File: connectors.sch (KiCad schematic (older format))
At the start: 15 parts, among them J1 2001-1-2-21-00-BK, P2 USB_A, P3 CAM1, Q3 2N7002P.215

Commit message: Assigned footprints to most components
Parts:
- removed D2, D3: BAT54, symbol D_Schottky
- added D2, D3: BAT54, TO_SOT_Packages_SMD:SOT-23, symbol D_Schottky_AAK
- C16: footprint (none) -> Capacitors_Tantalum_SMD:CP_Tantalum_Case-C_EIA-6032-28_Reflow
- C17: footprint (none) -> Capacitors_SMD:C_0603_HandSoldering
- D4, D5, D6, D7, Q3: footprint (none) -> TO_SOT_Packages_SMD:SOT-23
- P2: value USB_A -> HOST; footprint (none) -> Connectors:USB_A
- R4, R5, R6: footprint (none) -> Resistors_SMD:R_0603_HandSoldering
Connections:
- no-connect marks 1 -> 3
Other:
- moved on the sheet: C16, P2
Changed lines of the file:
@@
 L GND #PWR050
 U 1 1 5C1263C9
-P 1350 1650
-F 0 "#PWR050" H 1350 1400 50  0001 C CNN
-F 1 "GND" H 1350 1500 50  0000 C CNN
-F 2 "" H 1350 1650 50  0000 C CNN
-F 3 "" H 1350 1650 50  0000 C CNN
-	1    1350 1650
+P 1350 1700
+F 0 "#PWR050" H 1350 1450 50  0001 C CNN
+F 1 "GND" H 1350 1550 50  0000 C CNN
+F 2 "" H 1350 1700 50  0000 C CNN
+F 3 "" H 1350 1700 50  0000 C CNN
+	1    1350 1700
 	1    0    0    -1
 $EndComp
@@
 L GND #PWR051
 U 1 1 5C1263E1
-P 1600 1650
-F 0 "#PWR051" H 1600 1400 50  0001 C CNN
-F 1 "GND" H 1600 1500 50  0000 C CNN
-F 2 "" H 1600 1650 50  0000 C CNN
-F 3 "" H 1600 1650 50  0000 C CNN
-	1    1600 1650
-	1    0    0    -1
-$EndComp
-Text GLabel 1150 1150 3    60   Input ~ 0
+P 1600 1700
+F 0 "#PWR051" H 1600 1450 50  0001 C CNN
+F 1 "GND" H 1600 1550 50  0000 C CNN
+F 2 "" H 1600 1700 50  0000 C CNN
+F 3 "" H 1600 1700 50  0000 C CNN
+	1    1600 1700
+	1    0    0    -1
+$EndComp
+Text GLabel 1150 1200 3    60   Input ~ 0
 USB_DM
-Text GLabel 1250 1150 3    60   Input ~ 0
+Text GLabel 1250 1200 3    60   Input ~ 0
 USB_DP
 $Comp
 L +5V #PWR052
 U 1 1 5C126DDC
-P 650 700
-F 0 "#PWR052" H 650 550 50  0001 C CNN
-F 1 "+5V" H 650 840 50  0000 C CNN
-F 2 "" H 650 700 50  0000 C CNN
-F 3 "" H 650 700 50  0000 C CNN
-	1    650  700
+P 550 700
+F 0 "#PWR052" H 550 550 50  0001 C CNN
+F 1 "+5V" H 550 840 50  0000 C CNN
+F 2 "" H 550 700 50  0000 C CNN
+F 3 "" H 550 700 50  0000 C CNN
+	1    550  700
 	1    0    0    -1
 $EndComp
@@
 L CP1 C16
 U 1 1 5C1275E4
-P 650 1400
-F 0 "C16" H 675 1500 50  0000 L CNN
-F 1 "10uF" H 675 1300 50  0000 L CNN
-F 2 "" H 650 1400 50  0000 C CNN
-F 3 "" H 650 1400 50  0000 C CNN
-	1    650  1400
+P 650 1450
+F 0 "C16" H 675 1550 50  0000 L CNN
+F 1 "10uF" H 675 1350 50  0000 L CNN
+F 2 "Capacitors_Tantalum_SMD:CP_Tantalum_Case-C_EIA-6032-28_Reflow" H 650 1450 50  0001 C CNN
+F 3 "" H 650 1450 50  0000 C CNN
+	1    650  1450
 	1    0    0    -1
 $EndComp
@@
 L GND #PWR053
 U 1 1 5C127628
-P 650 1650
-F 0 "#PWR053" H 650 1400 50  0001 C CNN
-F 1 "GND" H 650 1500 50  0000 C CNN
-F 2 "" H 650 1650 50  0000 C CNN
-F 3 "" H 650 1650 50  0000 C CNN
-	1    650  1650
+P 650 1700
+F 0 "#PWR053" H 650 1450 50  0001 C CNN
+F 1 "GND" H 650 1550 50  0000 C CNN
+F 2 "" H 650 1700 50  0000 C CNN
+F 3 "" H 650 1700 50  0000 C CNN
+	1    650  1700
 	1    0    0    -1
 $EndComp
@@
 F 0 "P3" H 2100 2850 50  0000 C CNN
 F 1 "CAM1" V 2200 1700 50  0000 C CNN
-F 2 "" H 2100 1700 50  0000 C CNN
+F 2 "" H 2100 1700 50  0001 C CNN
 F 3 "" H 2100 1700 50  0000 C CNN
 	1    2100 1700
@@
 L USB_A P2
 U 1 1 5C12CE0A
-P 1250 750
-F 0 "P2" H 1450 550 50  0000 C CNN
-F 1 "USB_A" H 1200 950 50  0000 C CNN
-F 2 "" V 1200 650 50  0000 C CNN
-F 3 "" V 1200 650 50  0000 C CNN
-	1    1250 750
+P 1250 800
+F 0 "P2" H 1450 600 50  0000 C CNN
+F 1 "HOST" H 1200 1000 50  0000 C CNN
+F 2 "Connectors:USB_A" V 1200 700 50  0001 C CNN
+F 3 "" V 1200 700 50  0000 C CNN
+	1    1250 800
 	1    0    0    -1
 $EndComp
@@
 F 0 "D4" H 6100 3350 50  0000 C CNN
 F 1 "BAV99" H 6050 3550 50  0000 C CNN
-F 2 "" H 6050 3450 50  0000 C CNN
+F 2 "TO_SOT_Packages_SMD:SOT-23" H 6050 3450 50  0001 C CNN
 F 3 "" H 6050 3450 50  0000 C CNN
 	1    6050 3450
@@
 $EndComp
 $Comp
-L D_Schottky D3
-U 1 1 5C12B9C1
-P 5450 1550
-F 0 "D3" H 5450 1650 50  0000 C CNN
-F 1 "BAT54" H 5450 1450 50  0000 C CNN
-F 2 "" H 5450 1550 50  0000 C CNN
-F 3 "" H 5450 1550 50  0000 C CNN
-	1    5450 1550
-	0    -1   -1   0
-$EndComp
-$Comp
 L +5V #PWR056
 U 1 1 5C12BC08
-P 5450 700
-F 0 "#PWR056" H 5450 550 50  0001 C CNN
-F 1 "+5V" H 5450 840 50  0000 C CNN
-F 2 "" H 5450 700 50  0000 C CNN
-F 3 "" H 5450 700 50  0000 C CNN
-	1    5450 700
+P 5350 700
+F 0 "#PWR056" H 5350 550 50  0001 C CNN
+F 1 "+5V" H 5350 840 50  0000 C CNN
+F 2 "" H 5350 700 50  0000 C CNN
+F 3 "" H 5350 700 50  0000 C CNN
+	1    5350 700
 	1    0    0    -1
 $EndComp
@@
 F 0 "C17" H 5025 3550 50  0000 L CNN
 F 1 "100nF" H 5025 3350 50  0000 L CNN
-F 2 "" H 5038 3300 50  0000 C CNN
+F 2 "Capacitors_SMD:C_0603_HandSoldering" H 5038 3300 50  0001 C CNN
 F 3 "" H 5000 3450 50  0000 C CNN
 	1    5000 3450
@@
 F 0 "D5" H 6600 3350 50  0000 C CNN
 F 1 "BAV99" H 6550 3550 50  0000 C CNN
-F 2 "" H 6550 3450 50  0000 C CNN
+F 2 "TO_SOT_Packages_SMD:SOT-23" H 6550 3450 50  0001 C CNN
 F 3 "" H 6550 3450 50  0000 C CNN
 	1    6550 3450
@@
 F 0 "D6" H 7100 3350 50  0000 C CNN
 F 1 "BAV99" H 7050 3550 50  0000 C CNN
-F 2 "" H 7050 3450 50  0000 C CNN
+F 2 "TO_SOT_Packages_SMD:SOT-23" H 7050 3450 50  0001 C CNN
 F 3 "" H 7050 3450 50  0000 C CNN
 	1    7050 3450
@@
 F 0 "R4" V 6330 1550 50  0000 C CNN
 F 1 "1.8K" V 6250 1550 50  0000 C CNN
-F 2 "" V 6180 1550 50  0000 C CNN
+F 2 "Resistors_SMD:R_0603_HandSoldering" V 6180 1550 50  0001 C CNN
 F 3 "" H 6250 1550 50  0000 C CNN
 	1    6250 1550
@@
 F 0 "R5" V 6830 1550 50  0000 C CNN
 F 1 "1.8K" V 6750 1550 50  0000 C CNN
-F 2 "" V 6680 1550 50  0000 C CNN
+F 2 "Resistors_SMD:R_0603_HandSoldering" V 6680 1550 50  0001 C CNN
 F 3 "" H 6750 1550 50  0000 C CNN
 	1    6750 1550
@@
 HDMI_CLK_N
 $Comp
-L D_Schottky D2
-U 1 1 5C132132
-P 650 900
-F 0 "D2" H 650 1000 50  0000 C CNN
-F 1 "BAT54" H 650 800 50  0000 C CNN
-F 2 "" H 650 900 50  0000 C CNN
-F 3 "" H 650 900 50  0000 C CNN
-	1    650  900
-	0    -1   -1   0
-$EndComp
-$Comp
 L Q_NMOS_GSD Q3
 U 1 1 5C13782A
@@
 F 0 "Q3" H 8250 3500 50  0000 L CNN
 F 1 "2N7002P.215" H 8250 3400 50  0000 L CNN
-F 2 "" H 8250 3550 50  0000 C CNN
+F 2 "TO_SOT_Packages_SMD:SOT-23" H 8250 3550 50  0001 C CNN
 F 3 "" H 8050 3450 50  0000 C CNN
 	1    8050 3450
@@
 F 0 "R6" V 8230 2950 50  0000 C CNN
 F 1 "100K" V 8150 2950 50  0000 C CNN
-F 2 "" V 8080 2950 50  0000 C CNN
+F 2 "Resistors_SMD:R_0603_HandSoldering" V 8080 2950 50  0001 C CNN
 F 3 "" H 8150 2950 50  0000 C CNN
 	1    8150 2950
@@
 Connection ~ 5450 2850
 Wire Wire Line
-	5450 2850 5450 1700
-Wire Wire Line
-	5450 1400 5450 700
+	5350 1400 5350 700
 Wire Wire Line
 	4500 2250 4700 2250
@@
 	2300 650  2400 650
 Wire Wire Line
-	650  1550 650  1650
-Connection ~ 650  1150
-Wire Wire Line
-	650  750  650  700
-Wire Wire Line
-	650  1050 650  1250
-Wire Wire Line
-	650  1150 1050 1150
-Wire Wire Line
-	1050 1150 1050 1050
-Wire Wire Line
-	1250 1050 1250 1150
-Wire Wire Line
-	1150 1050 1150 1150
-Wire Wire Line
-	1600 650  1600 1650
-Wire Wire Line
-	1550 650  1600 650
-Wire Wire Line
-	1350 1650 1350 1050
+	650  1600 650  1700
+Connection ~ 650  1200
+Wire Wire Line
+	550  750  550  700
+Wire Wire Line
+	650  1100 650  1300
+Wire Wire Line
+	650  1200 1050 1200
+Wire Wire Line
+	1050 1200 1050 1100
+Wire Wire Line
+	1250 1100 1250 1200
+Wire Wire Line
+	1150 1100 1150 1200
+Wire Wire Line
+	1600 700  1600 1700
+Wire Wire Line
+	1550 700  1600 700
+Wire Wire Line
+	1350 1700 1350 1100
 $Comp
 L D_x2_Serial_AKC D7
@@
 F 0 "D7" H 7600 3350 50  0000 C CNN
 F 1 "BAV99" H 7550 3550 50  0000 C CNN
-F 2 "" H 7550 3450 50  0000 C CNN
+F 2 "TO_SOT_Packages_SMD:SOT-23" H 7550 3450 50  0001 C CNN
 F 3 "" H 7550 3450 50  0000 C CNN
 	1    7550 3450
@@
 L PWR_FLAG #FLG067
 U 1 1 5C13FE61
-P 850 750
-F 0 "#FLG067" H 850 845 50  0001 C CNN
-F 1 "PWR_FLAG" V 900 600 50  0000 C CNN
-F 2 "" H 850 750 50  0000 C CNN
-F 3 "" H 850 750 50  0000 C CNN
-	1    850  750
-	1    0    0    -1
-$EndComp
-Wire Wire Line
-	850  750  850  1150
-Connection ~ 850  1150
+P 850 800
+F 0 "#FLG067" H 850 895 50  0001 C CNN
+F 1 "PWR_FLAG" V 900 650 50  0000 C CNN
+F 2 "" H 850 800 50  0000 C CNN
+F 3 "" H 850 800 50  0000 C CNN
+	1    850  800
+	1    0    0    -1
+$EndComp
+Wire Wire Line
+	850  800  850  1200
+Connection ~ 850  1200
+$Comp
+L D_Schottky_AAK D3
+U 1 1 5C147BC1
+P 5450 1600
+F 0 "D3" H 5450 1700 50  0000 C CNN
+F 1 "BAT54" H 5450 1500 50  0000 C CNN
+F 2 "TO_SOT_Packages_SMD:SOT-23" H 5450 1600 50  0001 C CNN
+F 3 "" H 5450 1600 50  0000 C CNN
+	1    5450 1600
+	0    -1   -1   0
+$EndComp
+Wire Wire Line
+	5450 1750 5450 2850
+NoConn ~ 5450 1400
+$Comp
+L D_Schottky_AAK D2
+U 1 1 5C1483E3
+P 650 950
+F 0 "D2" H 650 1050 50  0000 C CNN
+F 1 "BAT54" H 650 850 50  0000 C CNN
+F 2 "TO_SOT_Packages_SMD:SOT-23" H 650 950 50  0001 C CNN
+F 3 "" H 650 950 50  0000 C CNN
+	1    650  950
+	0    -1   -1   0
+$EndComp
+NoConn ~ 650  750
 $EndSCHEMATC

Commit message: Added camera connector footprint
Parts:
- J1: footprint digikey-footprints:HDMI_Mini_Female_2001-1-2-21-00-BK -> digikey-footprints:HDMI_Female_DC3RX19JA3R1700
- P3: footprint (none) -> ffc_conn:FPC_22
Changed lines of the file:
@@
 F 0 "P3" H 2100 2850 50  0000 C CNN
 F 1 "CAM1" V 2200 1700 50  0000 C CNN
-F 2 "" H 2100 1700 50  0001 C CNN
+F 2 "ffc_conn:FPC_22" H 2100 1700 50  0001 C CNN
 F 3 "" H 2100 1700 50  0000 C CNN
 	1    2100 1700
@@
 F 0 "J1" H 3585 3545 60  0000 C CNN
 F 1 "2001-1-2-21-00-BK" V 3510 1095 60  0000 C CNN
-F 2 "digikey-footprints:HDMI_Mini_Female_2001-1-2-21-00-BK" H 4100 2250 60  0001 L CNN
+F 2 "digikey-footprints:HDMI_Female_DC3RX19JA3R1700" H 4100 2250 60  0001 L CNN
 F 3 "http://cnctech.us/pdfs/2001-1-2-21-00-BK.pdf" H 4100 2350 60  0001 L CNN
 F 4 "1175-1704-1-ND" H 4100 2450 60  0001 L CNN "Digi-Key_PN"

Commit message: Replaced HDMI connector
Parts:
- J1: footprint digikey-footprints:HDMI_Female_DC3RX19JA3R1700 -> HDMI_MOLEX:HDMI_MOLEX_471510001
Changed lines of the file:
@@
 F 0 "J1" H 3585 3545 60  0000 C CNN
 F 1 "2001-1-2-21-00-BK" V 3510 1095 60  0000 C CNN
-F 2 "digikey-footprints:HDMI_Female_DC3RX19JA3R1700" H 4100 2250 60  0001 L CNN
+F 2 "HDMI_MOLEX:HDMI_MOLEX_471510001" H 4100 2250 60  0001 L CNN
 F 3 "http://cnctech.us/pdfs/2001-1-2-21-00-BK.pdf" H 4100 2350 60  0001 L CNN
 F 4 "1175-1704-1-ND" H 4100 2450 60  0001 L CNN "Digi-Key_PN"

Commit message: Fixed fused
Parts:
- C17: footprint Capacitors_SMD:C_0603_HandSoldering -> Capacitors_SMD:C_0402
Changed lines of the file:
@@
 F 0 "C17" H 5025 3550 50  0000 L CNN
 F 1 "100nF" H 5025 3350 50  0000 L CNN
-F 2 "Capacitors_SMD:C_0603_HandSoldering" H 5038 3300 50  0001 C CNN
+F 2 "Capacitors_SMD:C_0402" H 5038 3300 50  0001 C CNN
 F 3 "" H 5000 3450 50  0000 C CNN
 	1    5000 3450

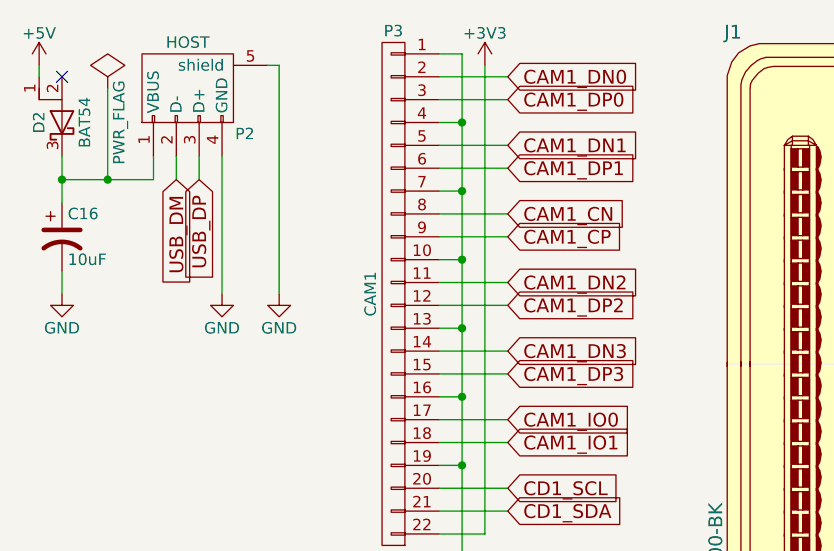
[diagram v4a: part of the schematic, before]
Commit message: Routed differential pairs for camera and HDMI
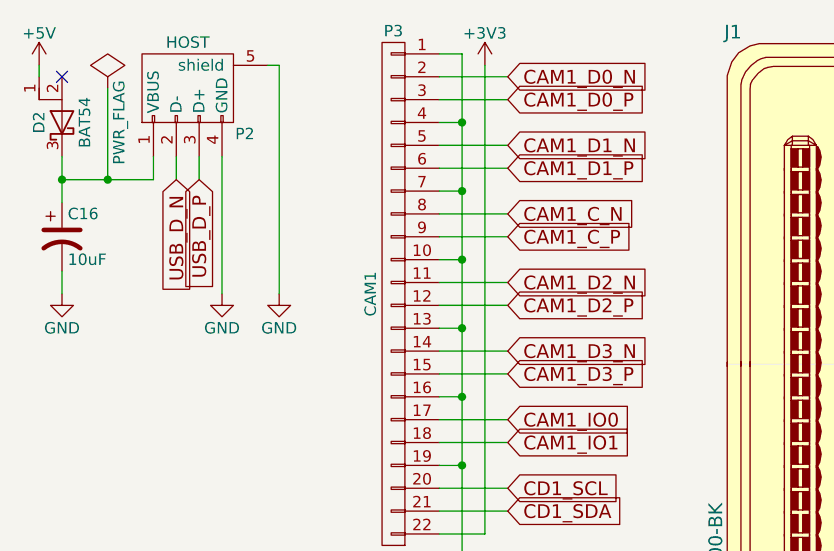
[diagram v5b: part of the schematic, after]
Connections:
- net CAM1_CN renamed CAM1_C_N
- net CAM1_CP renamed CAM1_C_P
- net CAM1_DN0 renamed CAM1_D0_N
- net CAM1_DN1 renamed CAM1_D1_N
- net CAM1_DN2 renamed CAM1_D2_N
- net CAM1_DN3 renamed CAM1_D3_N
- net CAM1_DP0 renamed CAM1_D0_P
- net CAM1_DP1 renamed CAM1_D1_P
- net CAM1_DP2 renamed CAM1_D2_P
- net CAM1_DP3 renamed CAM1_D3_P
- net USB_DM renamed USB_D_N
- net USB_DP renamed USB_D_P
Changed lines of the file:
@@
 $EndComp
 Text GLabel 1150 1200 3    60   Input ~ 0
-USB_DM
+USB_D_N
 Text GLabel 1250 1200 3    60   Input ~ 0
-USB_DP
+USB_D_P
 $Comp
 L +5V #PWR052
@@
 $EndComp
 Text GLabel 2600 750  2    60   Input ~ 0
-CAM1_DN0
+CAM1_D0_N
 Text GLabel 2600 850  2    60   Input ~ 0
-CAM1_DP0
+CAM1_D0_P
 Text GLabel 2600 1050 2    60   Input ~ 0
-CAM1_DN1
+CAM1_D1_N
 Text GLabel 2600 1150 2    60   Input ~ 0
-CAM1_DP1
+CAM1_D1_P
 Text GLabel 2600 1350 2    60   Input ~ 0
-CAM1_CN
+CAM1_C_N
 Text GLabel 2600 1450 2    60   Input ~ 0
-CAM1_CP
+CAM1_C_P
 Text GLabel 2600 1650 2    60   Input ~ 0
-CAM1_DN2
+CAM1_D2_N
 Text GLabel 2600 1750 2    60   Input ~ 0
-CAM1_DP2
+CAM1_D2_P
 Text GLabel 2600 1950 2    60   Input ~ 0
-CAM1_DN3
+CAM1_D3_N
 Text GLabel 2600 2050 2    60   Input ~ 0
-CAM1_DP3
+CAM1_D3_P
 Text GLabel 2600 2250 2    60   Input ~ 0
 CAM1_IO0

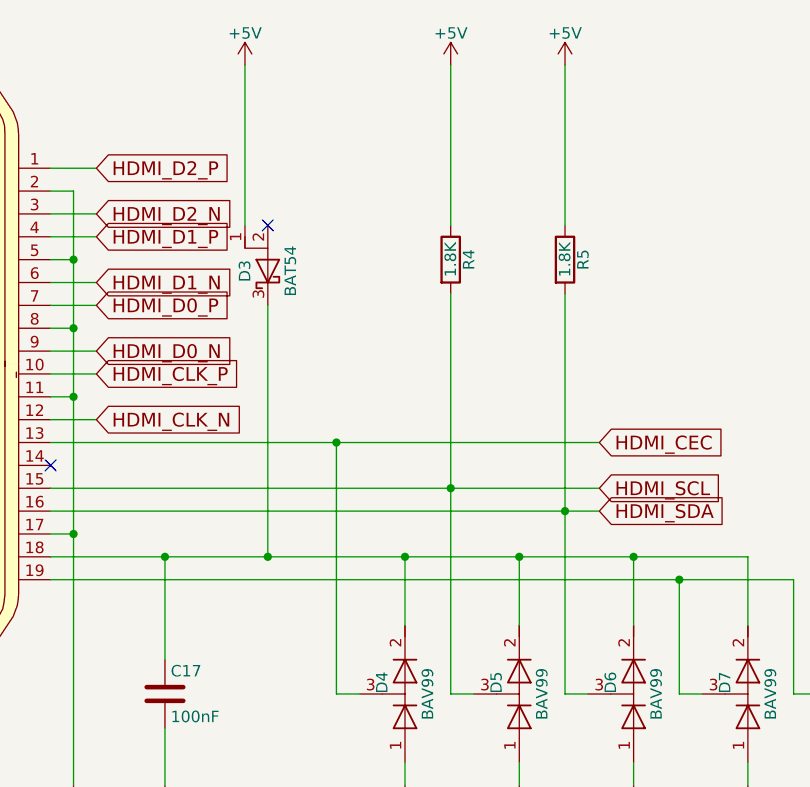
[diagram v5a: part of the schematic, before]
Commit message: Removed 2.5V regulator and changed bottom ground plane clearence
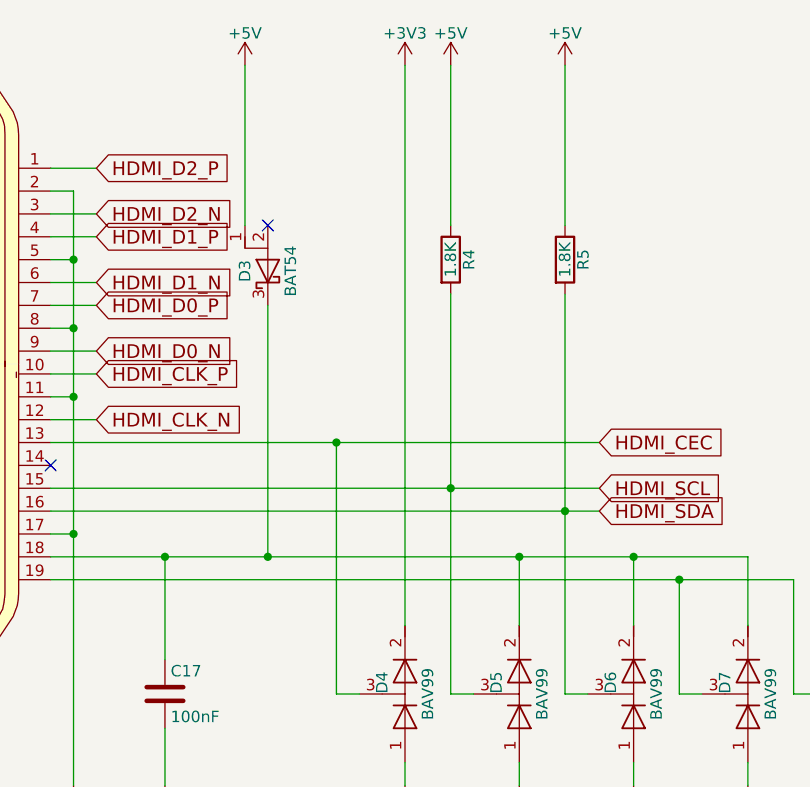
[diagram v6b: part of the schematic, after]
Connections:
- net +3V3: now also D4.2 (K)
- net at C17.1, D3.3 (K), D5.2 (K)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: no longer D4.2 (K)
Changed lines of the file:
@@
 	8150 2800 8150 2600
 Connection ~ 6550 2850
-Connection ~ 6050 2850
 Connection ~ 5450 2850
 Wire Wire Line
@@
 Wire Wire Line
 	6550 2850 6550 3150
-Wire Wire Line
-	6050 2850 6050 3150
 Wire Wire Line
 	6050 3850 6050 3750
@@
 $EndComp
 NoConn ~ 650  750
+$Comp
+L +3V3 #PWR?
+U 1 1 5C194AAE
+P 6050 700
+F 0 "#PWR?" H 6050 550 50  0001 C CNN
+F 1 "+3V3" H 6050 840 50  0000 C CNN
+F 2 "" H 6050 700 50  0000 C CNN
+F 3 "" H 6050 700 50  0000 C CNN
+	1    6050 700
+	1    0    0    -1
+$EndComp
+Wire Wire Line
+	6050 700  6050 3150
 $EndSCHEMATC
